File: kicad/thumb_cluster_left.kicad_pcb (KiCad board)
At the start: 2 copper layers, 41.2 x 43.8 mm, 16 parts, among them J1 Conn_01x07

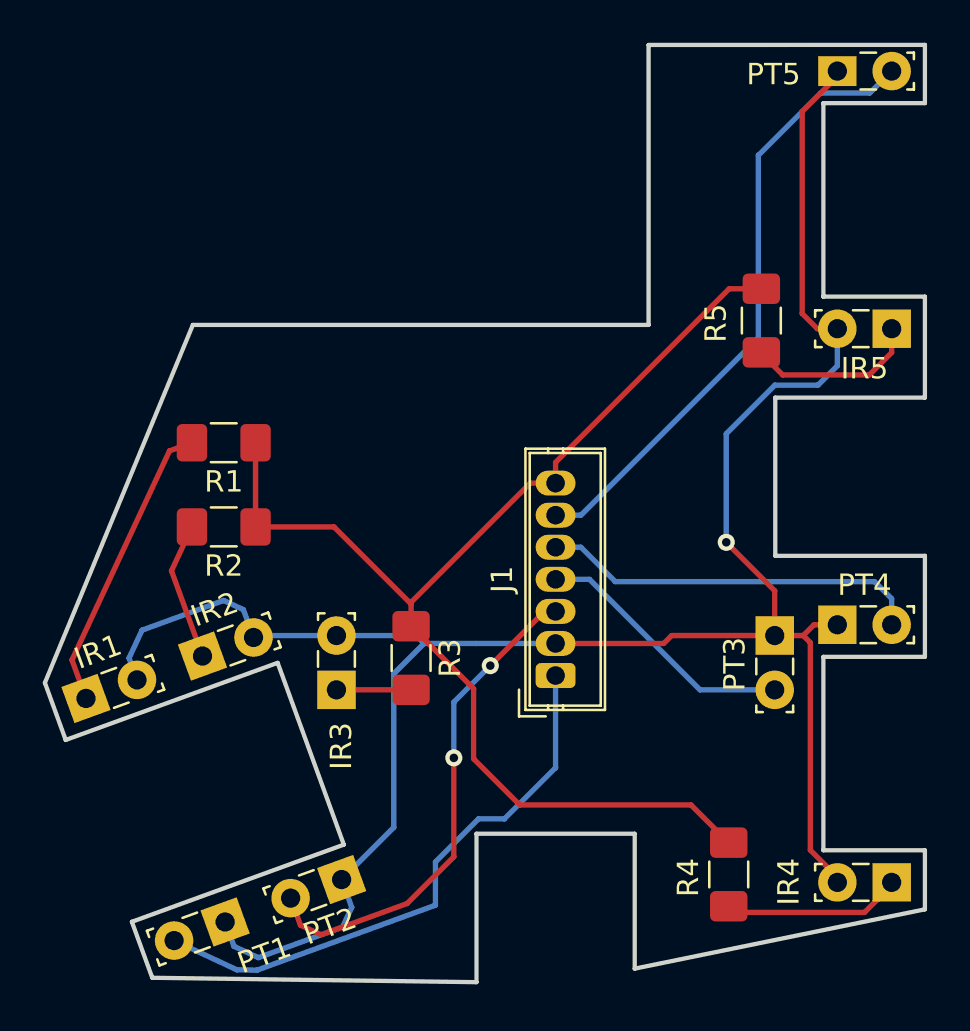
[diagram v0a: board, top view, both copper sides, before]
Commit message: Add a nub indicating the lens on the IR and PT footprints
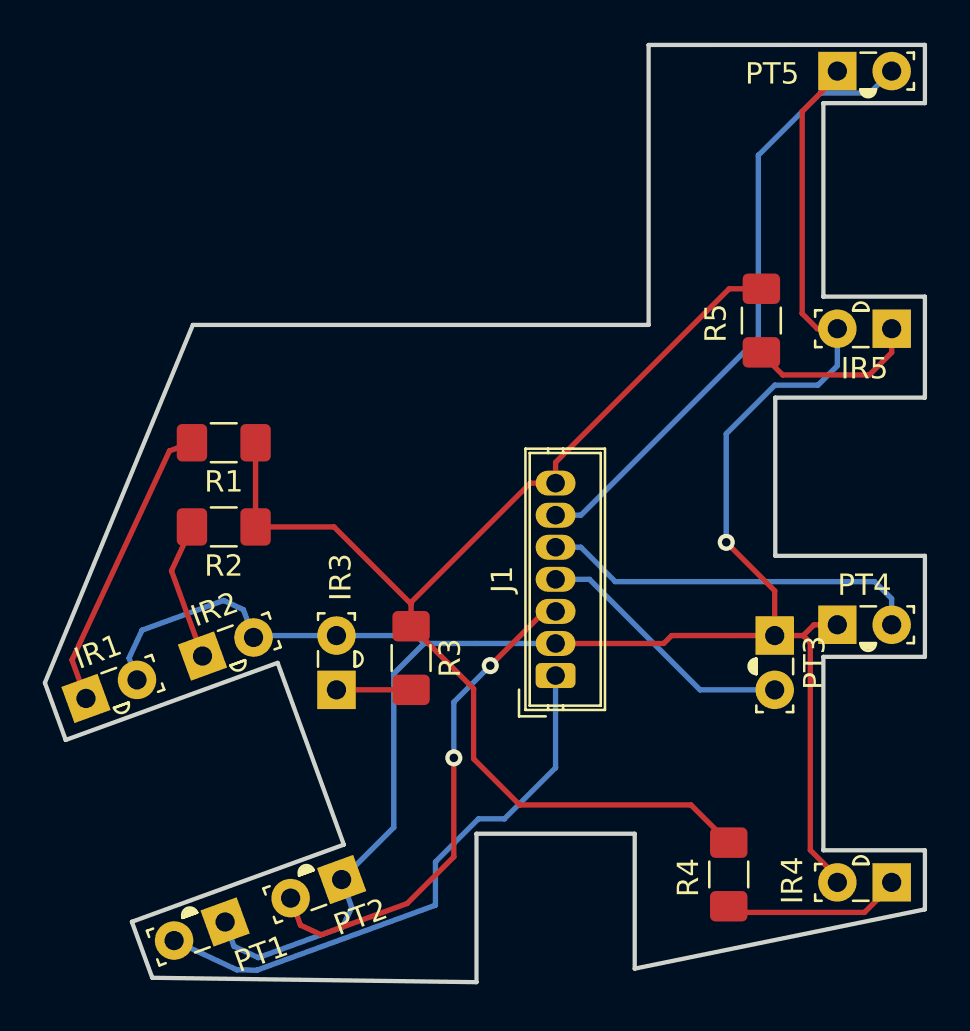
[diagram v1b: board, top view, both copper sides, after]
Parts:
- IR1, IR2, IR3, IR4, IR5: footprint LED_THT:LED_SideEmitter_Rectangular_W4.5mm_H1.6mm -> lalboard:IR908-7C-F
- PT1, PT2, PT3, PT4, PT5: footprint LED_THT:LED_SideEmitter_Rectangular_W4.5mm_H1.6mm -> lalboard:PT908-7C-F

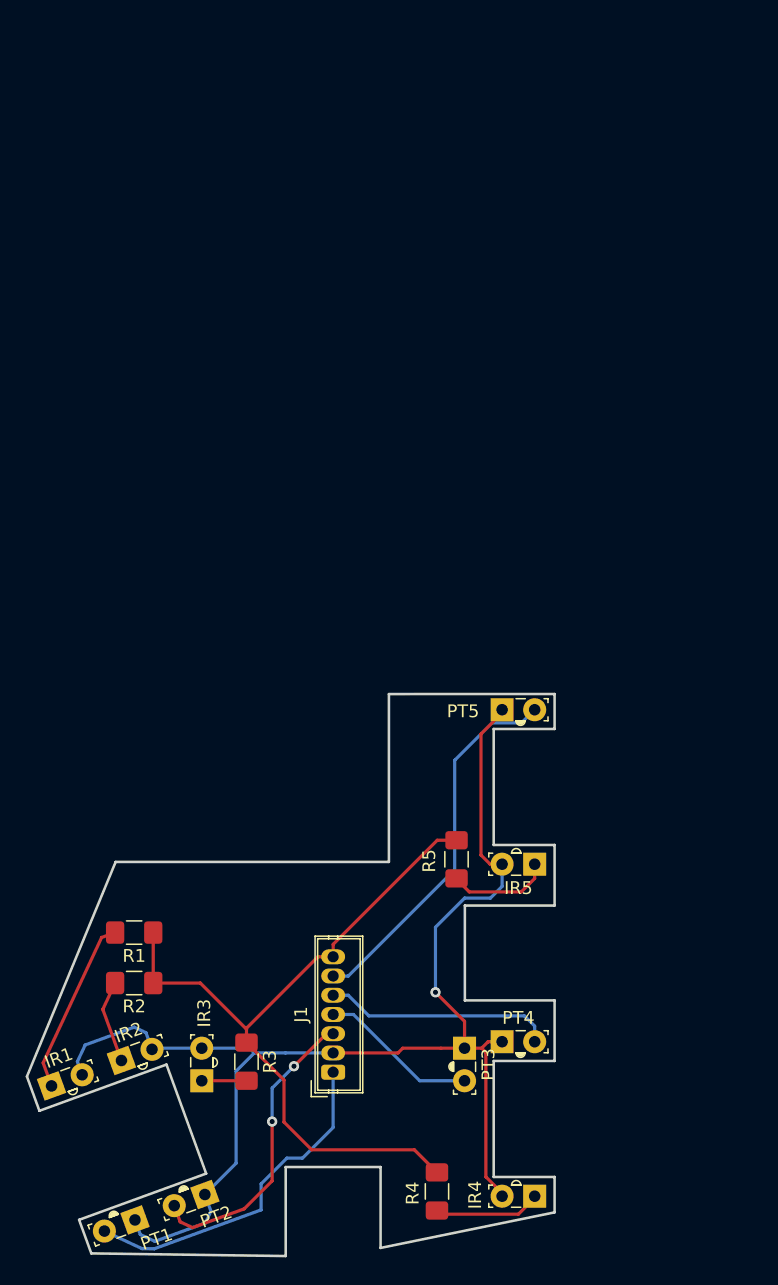
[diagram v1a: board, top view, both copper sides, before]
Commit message: Update the design of the left thumb cluster pcb
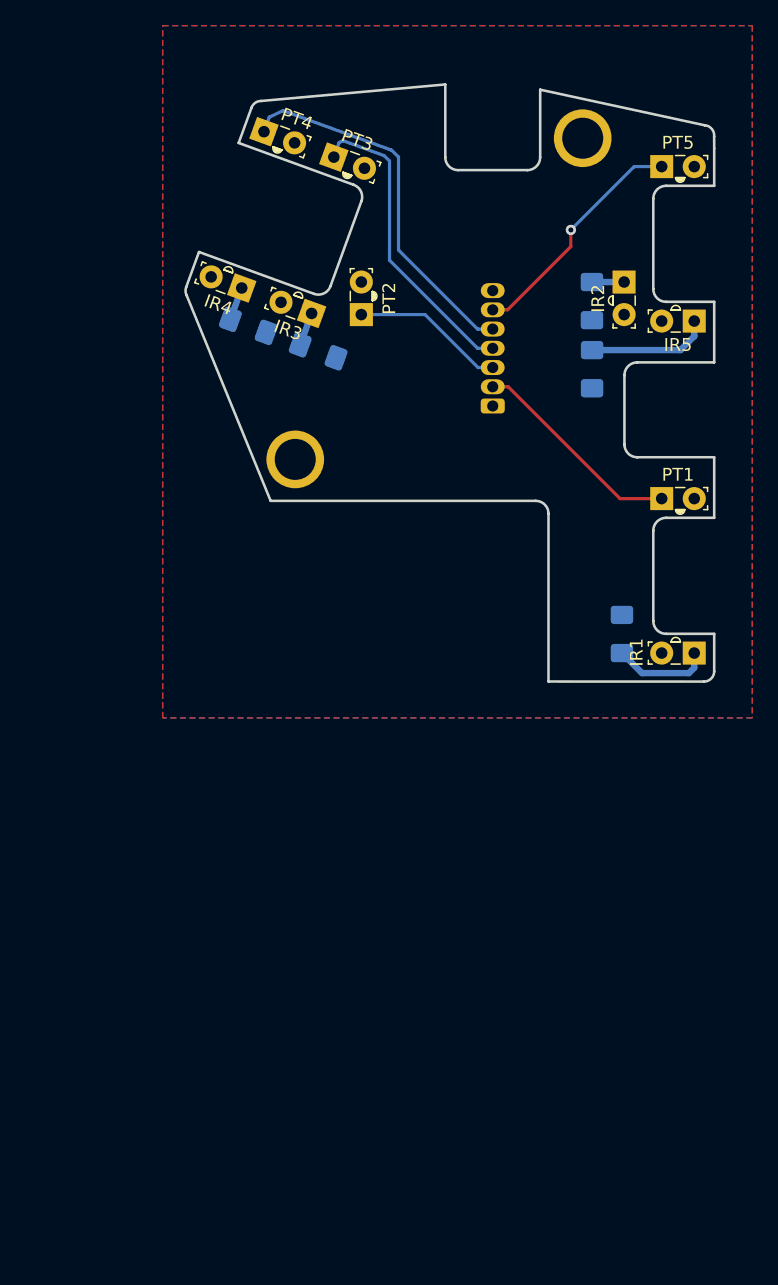
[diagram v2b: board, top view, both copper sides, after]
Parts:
- added ?: , , F.Cu at (169.1, 104.7)
- added ?: , , F.Cu at (168.1, 101.4)
- added REF**: MountingHole_3.2mm_M3_Pad, MountingHole:MountingHole_3.2mm_M3_Pad, F.Cu at (141.8, 91.4)
- added REF**: MountingHole_3.2mm_M3_Pad, MountingHole:MountingHole_3.2mm_M3_Pad, F.Cu at (164.3, 66.3)
- J1, R2, R3, R4, R5: moved to B.Cu
- R1: value 150 -> 100; moved to B.Cu
- moved IR4 74.4 mm to (137.7, 78.0), turned to 160 degrees
- moved PT4 73.4 mm to (139.4, 65.8), turned to 340 degrees
- moved IR2 72.3 mm to (167.5, 77.5), turned to 270 degrees
- moved PT3 70.3 mm to (144.9, 67.8), turned to 340 degrees
- moved PT2 69.7 mm to (147.0, 80.1), turned to 90 degrees
- moved PT1 69.7 mm to (170.4, 94.4), turned to 0 degrees
- moved R4 69.1 mm to (138.2, 80.9), turned to 160 degrees
- moved R2 64.1 mm to (165.0, 79.0), turned to 90 degrees
- moved IR3 60.5 mm to (143.1, 80.0), turned to 160 degrees
- moved IR1 60.4 mm to (173.0, 106.5), turned to 180 degrees
- moved R3 55.7 mm to (143.6, 82.9), turned to 160 degrees
- moved J1 53.4 mm to (157.2, 87.2)
- moved R1 44.6 mm to (167.3, 105.0), turned to 270 degrees
- moved PT5 44.2 mm to (170.4, 68.5)
- moved IR5 44.2 mm to (173.0, 80.6)
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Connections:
- J1 pad 1: C1 -> +5V
- J1 pad 2: +5V -> C1
- J1 pad 3: C3 -> C2
- J1 pad 4: C4 -> C3
- J1 pad 5: C5 -> C4
- J1 pad 6: C6 -> C5
- PT1 pad 1: +5V -> C1
- PT1 pad 2: C1 -> +5V
- PT2 pad 1: +5V -> C2
- PT2 pad 2: C3 -> +5V
- PT3 pad 1: +5V -> C3
- PT3 pad 2: C4 -> +5V
- PT4 pad 1: +5V -> C4
- PT4 pad 2: C5 -> +5V
- PT5 pad 1: +5V -> C5
- PT5 pad 2: C6 -> +5V
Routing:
- net +5V: track 103.3 -> 0.00 mm, vias 1 -> 0
- net GND: track 57.8 -> 0.00 mm
- net C6: track 29.3 -> 0.00 mm
- net C4: track 12.4 -> 29.3 mm
- net C2: track 0.00 -> 12.0 mm
- net C1: track 26.8 -> 17.2 mm
- net Net-(IR1-Pad1): track 13.8 -> 7.61 mm
- net Net-(IR4-Pad1): track 8.40 -> 2.60 mm
- net Net-(IR2-Pad1): track 6.51 -> 2.51 mm
- net Net-(IR5-Pad1): track 8.11 -> 9.60 mm
- net C5: track 17.9 -> 19.3 mm, vias 0 -> 1
- net Net-(IR3-Pad1): track 3.49 -> 2.60 mm
- net C3: track 23.6 -> 24.2 mm, vias 2 -> 0
- added copper zone on F.Cu, net +5V
- added copper zone on B.Cu, net GND
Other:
- board size 41.2 x 43.8 mm -> 41.2 x 46.6 mm
- net class Power added: clearance 0.2, trace_width 0.5, via_dia 0.8, via_drill 0.4
- board text added: "100"
- board text added: "150"
- board text added: "Coords for import: (100, 150)"
- board text added: "Max internal corner radius: 1.0mm (for all internal corners)"
- board text added: "lalboard.com left thumb cluster v0.1"

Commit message: Fix up the cluster and thumb_cluster_left pcbs
Some of the nets for the pours and screw holes had gotten unassigned
somehow
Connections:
- REF** pad 1: (no net) -> GND (x2)
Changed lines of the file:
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@@
     (visible_elements FFFFFF7F)
     (pcbplotparams
-      (layerselection 0x010fc_ffffffff)
+      (layerselection 0x210fc_ffffffff)
       (usegerberextensions false)
       (usegerberattributes true)
@@
       (outputformat 1)
       (mirror false)
-      (drillshape 1)
+      (drillshape 0)
       (scaleselection 1)
-      (outputdirectory ""))
+      (outputdirectory "/tmp/thumb_cluster_left/"))
   )
   (net 0 "")
@@
       (effects (font (size 1 1) (thickness 0.15)))
     )
-    (pad 1 thru_hole circle (at 0 0) (size 4.5 4.5) (drill 3.2) (layers *.Cu *.Mask))
+    (pad 1 thru_hole circle (at 0 0) (size 4.5 4.5) (drill 3.2) (layers *.Cu *.Mask)
+      (net 7 GND))
   )
   (module Resistor_SMD:R_1206_3216Metric_Pad1.42x1.75mm_HandSolder (layer B.Cu)
@@
       (effects (font (size 1 1) (thickness 0.15)))
     )
-    (pad 1 thru_hole circle (at 0 0 180) (size 4.5 4.5) (drill 3.2) (layers *.Cu *.Mask))
+    (pad 1 thru_hole circle (at 0 0 180) (size 4.5 4.5) (drill 3.2) (layers *.Cu *.Mask)
+      (net 7 GND))
   )
   (module Resistor_SMD:R_1206_3216Metric_Pad1.42x1.75mm_HandSolder (layer B.Cu)

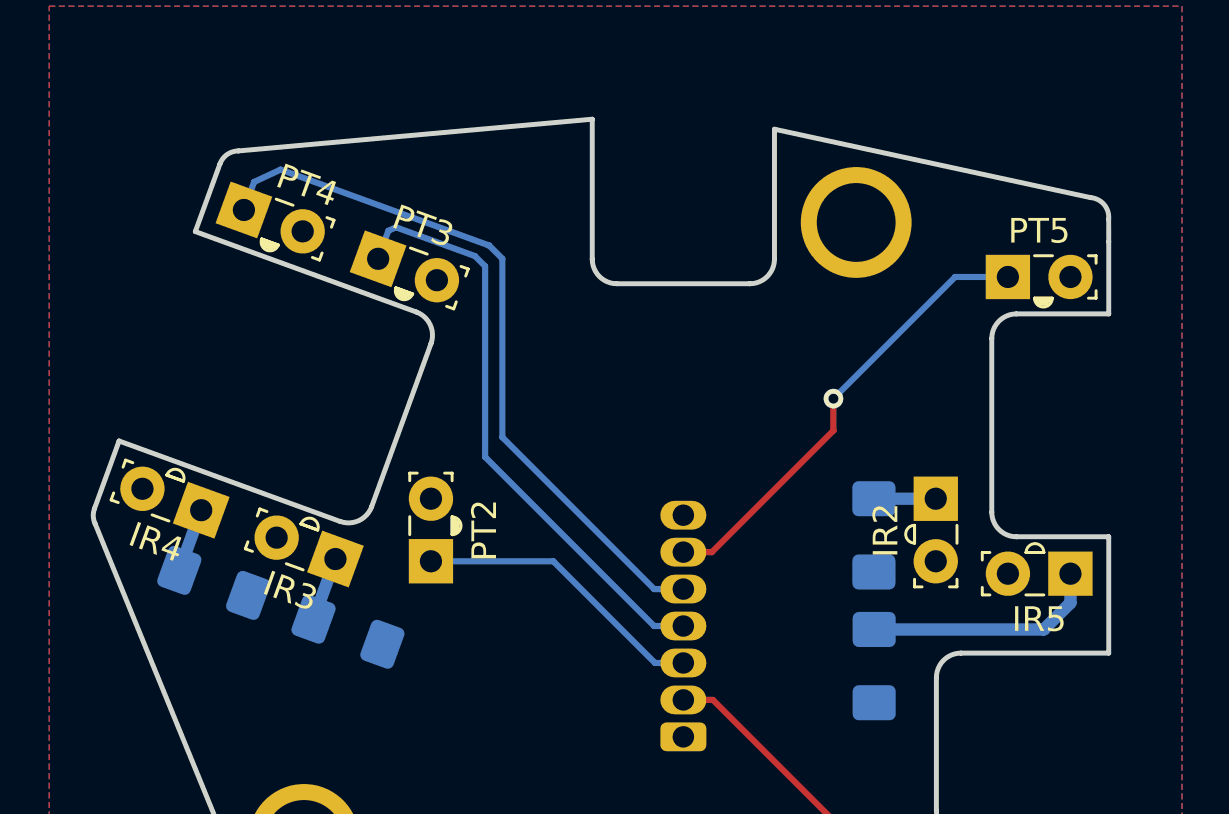
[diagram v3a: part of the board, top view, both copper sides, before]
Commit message: Update thumb cluster pcbs to v0.2
This shuffles the switch numbering and order on the connector,
so that the center key is on the same pin of the connector (pin 4)
as the center key of the finger clusters.

These keys on the thumb and finger clusters have inverted logic from
all the other keys, due to the physical design of the switches. This
puts the inverted keys on the same pin/column. This simplifies the
firmware a bit, because it can just assume that pin is always inverted.
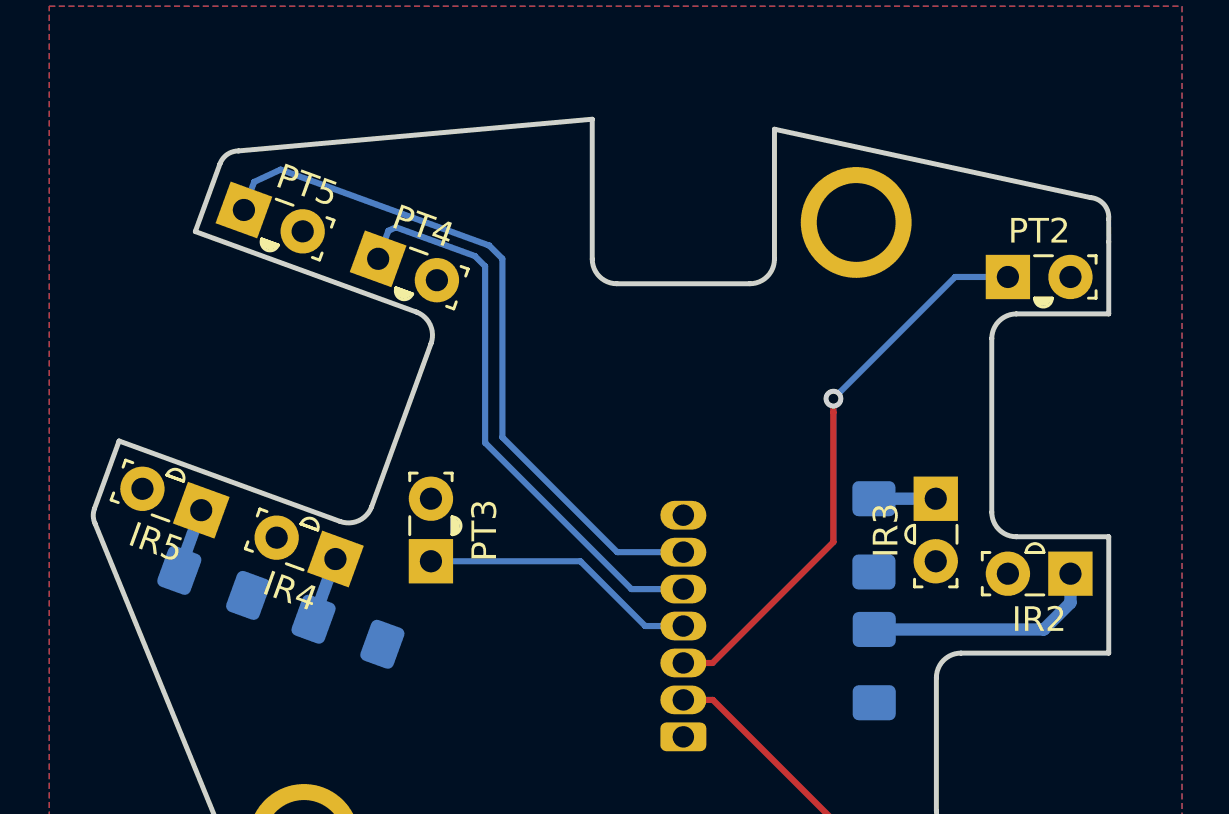
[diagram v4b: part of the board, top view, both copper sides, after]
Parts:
- removed ? (x2): , 
- removed the PT2 at (147.0, 80.1)
- removed the R3 at (143.6, 82.9)
- added PT3: PT908-7B-F, lalboard:PT908-7C-F, F.Cu at (147.0, 80.1)
- added R4: 150, Resistor_SMD:R_1206_3216Metric_Pad1.42x1.75mm_HandSolder, B.Cu at (143.6, 82.9)
- H1, H2: renamed from REF**; value MountingHole_3.2mm_M3_Pad -> MountingHole_Pad
- renumbered IR5 to IR2, IR2 to IR3, IR3 to IR4, IR4 to IR5, PT5 to PT2, PT3 to PT4, PT4 to PT5, R5 to R2, R2 to R3, R4 to R5
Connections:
- PT2 pad 1: C5 -> C2
- PT4 pad 1: C3 -> C4
- PT5 pad 1: C4 -> C5
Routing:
- net C3: track 24.2 -> 11.3 mm
- net C2: track 12.0 -> 23.1 mm, vias 0 -> 1
- net C5: track 19.3 -> 29.5 mm, vias 1 -> 0
- net C4: track 29.3 -> 23.2 mm
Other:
- board text added: "lalboard.com left thumb cluster v0.2"
- board text removed: "lalboard.com left thumb cluster v0.1"

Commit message: Update the various sensitivity-related resistor values
This updates the transimpedance amplifier resistors to 2k, and adjusts
the LED drive resistors to an appropriate level, from empirical testing.
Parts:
- R1: value 100 -> 56
- R2: value 150 -> 100
- R3: value 150 -> 120
- R4: value 150 -> 180
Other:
- board text removed: "100"
- board text removed: "150"
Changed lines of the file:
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@@
   (general
     (thickness 1.6)
-    (drawings 124)
+    (drawings 119)
     (tracks 41)
     (zones 0)
@@
       (effects (font (size 1 1) (thickness 0.15)) (justify mirror))
     )
-    (fp_text value 100 (at 0 1.651651 90) (layer B.Fab)
+    (fp_text value 56 (at 0 1.651651 90) (layer B.SilkS)
       (effects (font (size 1 1) (thickness 0.15)) (justify mirror))
     )
@@
       (effects (font (size 1 1) (thickness 0.15)) (justify mirror))
     )
-    (fp_text value 150 (at 0 -1.82 160) (layer B.Fab)
+    (fp_text value 150 (at 0.054082 -1.671412 160) (layer B.SilkS)
       (effects (font (size 1 1) (thickness 0.15)) (justify mirror))
     )
@@
       (effects (font (size 1 1) (thickness 0.15)) (justify mirror))
     )
-    (fp_text value 150 (at 0 -1.82 90) (layer B.Fab)
+    (fp_text value 100 (at 0 -1.599999 90) (layer B.SilkS)
       (effects (font (size 1 1) (thickness 0.15)) (justify mirror))
     )
@@
       (effects (font (size 1 1) (thickness 0.15)) (justify mirror))
     )
-    (fp_text value 150 (at 0 -1.82 90) (layer B.Fab)
+    (fp_text value 120 (at 0 -1.588979 90) (layer B.SilkS)
       (effects (font (size 1 1) (thickness 0.15)) (justify mirror))
     )
@@
       (effects (font (size 1 1) (thickness 0.15)) (justify mirror))
     )
-    (fp_text value 150 (at 0 -1.82 160) (layer B.Fab)
+    (fp_text value 180 (at 0.048513 -1.686714 160) (layer B.SilkS)
       (effects (font (size 1 1) (thickness 0.15)) (justify mirror))
     )
@@
     )
   )
-  (gr_text 150 (at 142.968185 84.573011 -20) (layer B.SilkS)
-    (effects (font (size 1 1) (thickness 0.15)) (justify mirror))
-  )
   (gr_text "lalboard.com\nleft thumb cluster\nv0.2" (at 154.978348 72.71453) (layer B.SilkS)
     (effects (font (size 1 1) (thickness 0.15)) (justify mirror))
@@
   (gr_line (start 174.524999 91.198958) (end 168.524999 91.198959) (layer Edge.Cuts) (width 0.2))
   (gr_arc (start 168.524999 90.19896) (end 167.524999 90.198959) (angle -90) (layer Edge.Cuts) (width 0.2))
-  (gr_text 100 (at 165.545154 104.966079 90) (layer B.SilkS)
-    (effects (font (size 1 1) (thickness 0.15)) (justify mirror))
-  )
-  (gr_text 150 (at 163.345155 84.266079 90) (layer B.SilkS)
-    (effects (font (size 1 1) (thickness 0.15)) (justify mirror))
-  )
-  (gr_text 150 (at 163.345154 78.966078 90) (layer B.SilkS)
-    (effects (font (size 1 1) (thickness 0.15)) (justify mirror))
-  )
   (gr_line (start 138.431984 63.932997) (end 137.431575 66.681598) (layer Edge.Cuts) (width 0.2))
   (gr_line (start 137.431575 66.681598) (end 146.405641 69.94789) (layer Edge.Cuts) (width 0.2))
@@
   (gr_line (start 174.525 95.922918) (end 174.524999 91.198958) (layer Edge.Cuts) (width 0.2))
   (gr_line (start 174.524999 83.798959) (end 174.524999 79.074999) (layer Edge.Cuts) (width 0.2))
-  (gr_text 150 (at 137.517968 82.589293 -20) (layer B.SilkS)
-    (effects (font (size 1 1) (thickness 0.15)) (justify mirror))
-  )
   (gr_line (start 167.524999 90.198959) (end 167.524999 84.798959) (layer Edge.Cuts) (width 0.2))
   (gr_arc (start 168.525 84.798959) (end 168.525 83.798959) (angle -90) (layer Edge.Cuts) (width 0.2))
